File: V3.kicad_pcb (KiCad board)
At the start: 2 copper layers, 128.2 x 59 mm, 105 parts, among them IC1 TPS62840DLCR","TPS62840DLCR, J1 Conn_01x04, J2 Conn_01x04, J3 FFC2B28-24-G, J6 Conn_01x02, J7 Conn_01x02, Q1 FDN304P","FDN304P, Q2 FDN304P","FDN304P, Q3 FDN304P","FDN304P, Q4 FDN304P","FDN304P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

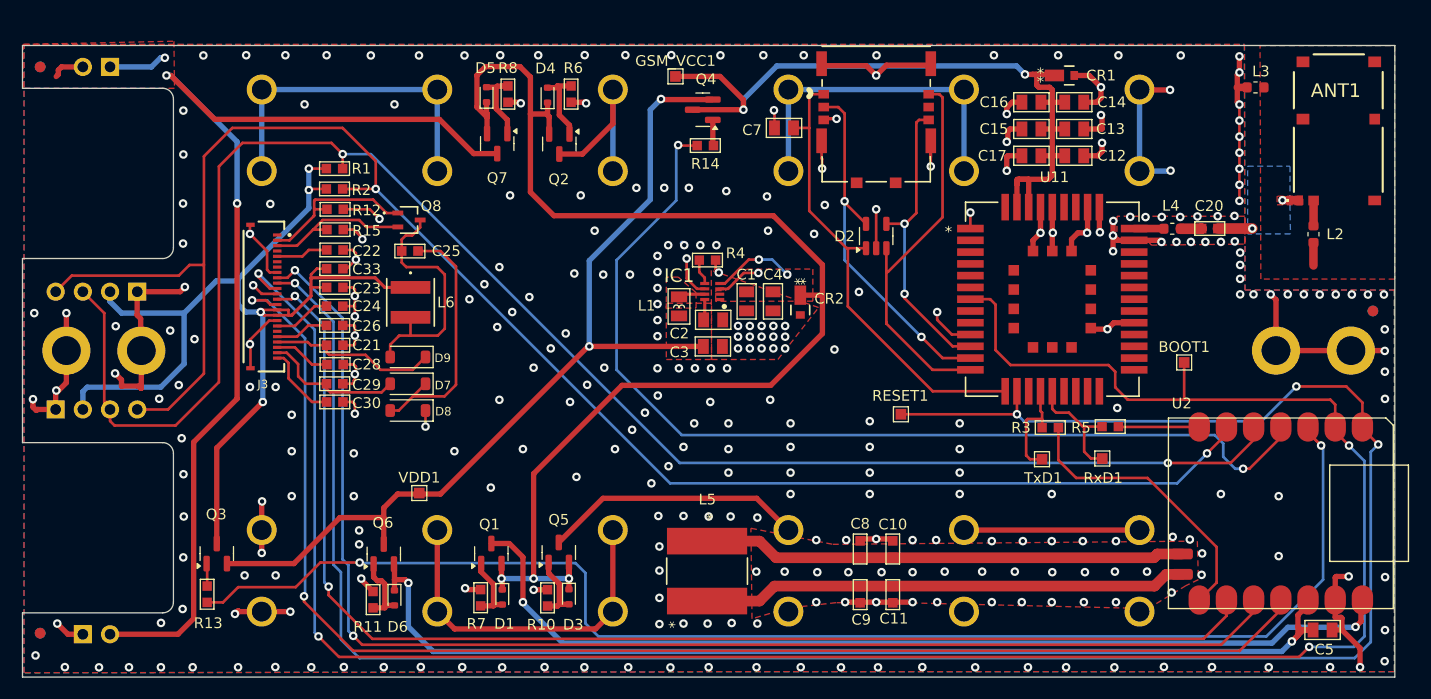
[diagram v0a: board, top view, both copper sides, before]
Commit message: add resisors to sim card, move TVS diode, add 3rd i2c header
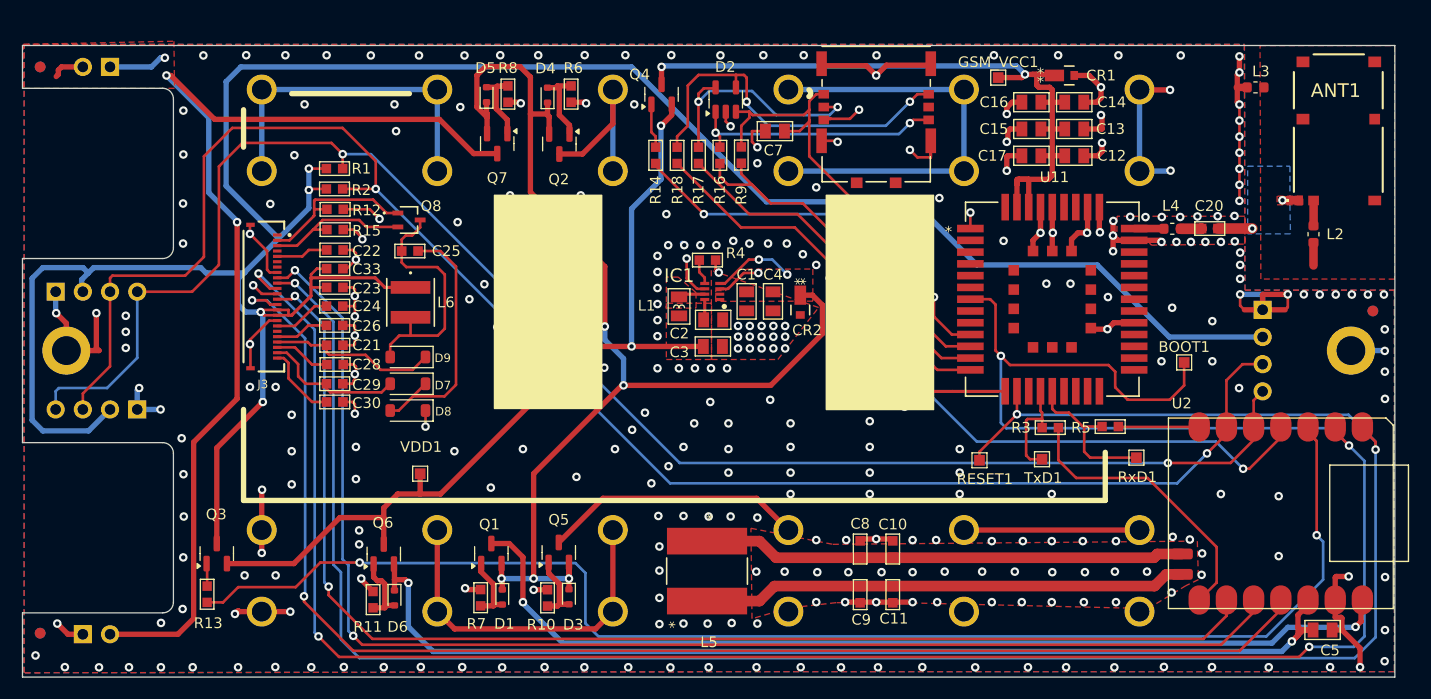
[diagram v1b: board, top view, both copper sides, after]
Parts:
- removed H3, H8: MountingHole_Pad_MP, MountingHole:MountingHole_2.7mm_M2.5_ISO14580_Pad
- added J4: Conn_01x04, Connector_PinSocket_2.54mm:PinSocket_1x04_P2.54mm_Vertical, B.Cu at (51.8, -3.81)
- added R16: 22R","22R, kicad_mod:R0603, F.Cu at (1.05, -18.2)
- added R17: 22R","22R, kicad_mod:R0603, F.Cu at (-0.95, -18.2)
- added R18: 22R","22R, kicad_mod:R0603, F.Cu at (-2.95, -18.2)
- added R9: 10K","RC0603JR-0710KL, kicad_mod:R0603, F.Cu at (3.05, -18.3)
- C10, C11: value ~ -> 3.6pF","CBR06C369B5GAC
- C5, C7: footprint OPL_Capacitor:C0805 -> kicad_mod:C0805
- C8, C9: value 335pF","GCM1885C2A331JA16D -> 51pF","06031U510GAT2A
- moved G*** 57.2 mm to (56.0, -17.0), turned to -90 degrees
- moved GSM_VCC1 30.2 mm to (27.1, -25.5)
- moved D2 19.0 mm to (1.60, -23.4)
- moved RESET1 8.51 mm to (25.3, 10.2)
- moved J1 7.62 mm to (-53.4, 5.50), turned to 90 degrees
- moved J2 7.62 mm to (-61.0, -5.50), turned to -90 degrees
- moved R14 4.73 mm to (-4.95, -18.2), turned to 90 degrees
- moved Q4 4.11 mm to (-4.40, -23.9), turned to 90 degrees
- moved RxD1 3.19 mm to (40.0, 10.0)
- moved VDD1 1.81 mm to (-26.9, 11.5)
- moved C7 0.90 mm to (6.19, -20.5)
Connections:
- D2 pad 1: SIM_VCC -> TVS_IO
- D2 pad 3: SIM_CLK -> SIM_VCC
- D2 pad 4: SIM_IO -> TVS_CLK
- D2 pad 5: SIM_RST -> TVS_RST
- J1 pad 3: SDA -> SCL
- J1 pad 4: SCL -> SDA
- J2 pad 3: SDA -> SCL
- J2 pad 4: SCL -> SDA
- U12 pad S2: SIM_RST -> TVS_RST
- U12 pad S3: SIM_CLK -> TVS_CLK
- U12 pad S6: SIM_IO -> TVS_IO
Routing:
- net CO2_VCC: track 99.8 -> 237.4 mm
- net TVS_CLK: track 0.00 -> 34.9 mm, vias 0 -> 2
- net TVS_IO: track 0.00 -> 24.0 mm, vias 0 -> 2
- net TVS_RST: track 0.00 -> 22.7 mm, vias 0 -> 2
- net DISPLAY_DC: track 205.5 -> 227.9 mm, vias 4 -> 5
- net SIM_VCC: track 43.7 -> 62.9 mm, vias 0 -> 2
- net GSM_PWR: track 93.0 -> 77.6 mm
- net +BATT: track 130.0 -> 118.1 mm, vias 5 -> 7
- net Net-(U7-Pad1): track 31.6 -> 40.4 mm
- net SIM_IO: track 27.9 -> 35.7 mm, vias 2 -> 0
- net SDA: track 158.0 -> 150.5 mm
- net GND: track 248.6 -> 241.7 mm, vias 325 -> 344
- net DISPLAY_RST: track 204.9 -> 198.1 mm, vias 4 -> 3
- net VDD: track 88.4 -> 83.8 mm
- net GSM_VCC: track 72.2 -> 69.0 mm
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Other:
- board text added: "ComplexityMadeSimple.com"
- board text removed: "ComplexityMadeSimple.com MoistureIQ V1.0"

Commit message: add resistors for sim card. Move componets from sticky pads, make extra room for sim card holder
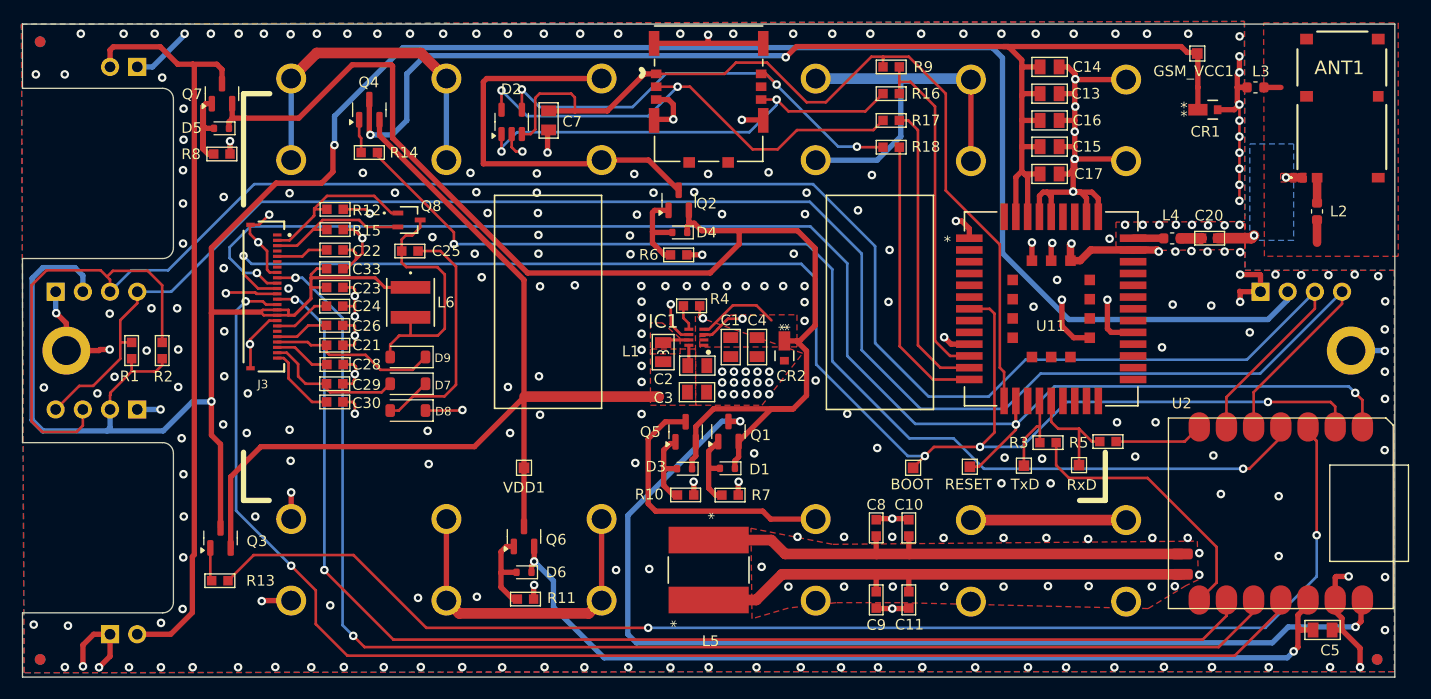
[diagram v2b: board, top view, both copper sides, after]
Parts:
- removed C12: 10uF","EMK212BJ106KG-T, kicad_mod:C0805
- moved FID4 32.6 mm to (62.5, 28.9)
- moved FID5 32.6 mm to (62.5, 28.9)
- moved G*** 32.2 mm to (55.0, 15.2)
- moved Q4 27.3 mm to (-31.7, -22.5)
- moved R8 27.3 mm to (-45.5, -18.4), turned to 180 degrees
- moved BOOT 27.2 mm to (19.1, 10.9)
- moved R14 26.8 mm to (-31.7, -18.5), turned to 180 degrees
- moved Q7 26.1 mm to (-45.5, -24.0), turned to 90 degrees
- moved R1 25.5 mm to (-53.9, 0.00), turned to -90 degrees
- moved R7 25.2 mm to (2.00, 13.5), turned to 180 degrees
- moved D5 25.0 mm to (-45.5, -20.8), turned to 180 degrees
- moved Q1 24.9 mm to (1.85, 7.56)
- moved D1 24.2 mm to (1.75, 11.0), turned to 180 degrees
- moved R2 22.1 mm to (-51.0, 0.00), turned to -90 degrees
- moved C7 21.2 mm to (-14.9, -21.5), turned to -90 degrees
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- renumbered BOOT1 to BOOT, RESET1 to RESET, RxD1 to RxD, TxD1 to TxD
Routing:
- net DISPLAY_DC: track 227.9 -> 141.5 mm, vias 5 -> 4
- net DISPLAY_RST: track 198.1 -> 141.1 mm
- net GSM_VCC: track 69.0 -> 122.1 mm
- net SCL: track 157.6 -> 190.7 mm, vias 2 -> 0
- net Vin3: track 100.6 -> 71.7 mm, vias 2 -> 0
- net GSM_PWR: track 77.6 -> 103.4 mm
- net TVS_RST: track 22.7 -> 45.1 mm
- net SIM_VCC: track 62.9 -> 85.3 mm, vias 2 -> 0
- net Vin2: track 17.0 -> 37.9 mm
- net TVS_IO: track 24.0 -> 42.4 mm
- net SDA: track 150.5 -> 165.9 mm, vias 2 -> 0
- net MCU_3V3: track 99.8 -> 85.3 mm
- net +BATT: track 118.1 -> 129.7 mm, vias 7 -> 0
- net VDD: track 83.8 -> 95.2 mm, vias 2 -> 0
- net SIM_CLK: track 35.4 -> 26.3 mm
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- removed copper zone on F.Cu, net Vin3
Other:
- board size 128.2 x 59 mm -> 128.2 x 61 mm

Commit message: ordred 23/10/2024
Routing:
- net GND: track 235.0 -> 240.2 mm, vias 304 -> 336
- net SIM_VCC: track 85.3 -> 89.3 mm
- net DISPLAY_SCK: track 117.7 -> 119.1 mm
- net CO2_VCC: track 238.8 -> 237.9 mm
- net GSM_VCC: track 122.1 -> 122.9 mm
- net TVS_RST: track 45.1 -> 46.0 mm
- net DISPLAY_DC: track 141.5 -> 140.7 mm
- net GSM_PWR: track 103.4 -> 102.8 mm
- net Net-(ANT1-FEED_(50_OHM)): track 5.02 -> 5.60 mm
- net MCU_3V3: track 85.3 -> 85.8 mm
- net DISPLAY_MOSI: track 129.8 -> 130.4 mm

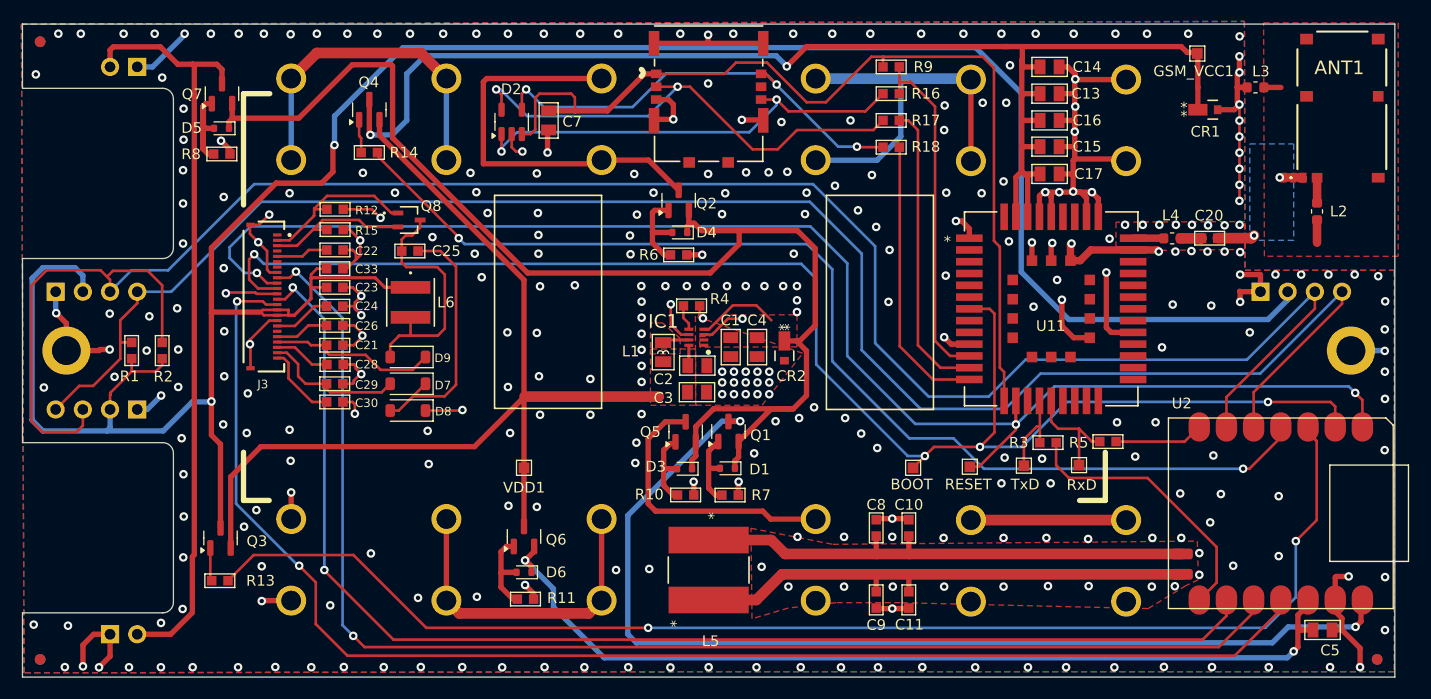
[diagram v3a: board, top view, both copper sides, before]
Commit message: change OR ring to diodes
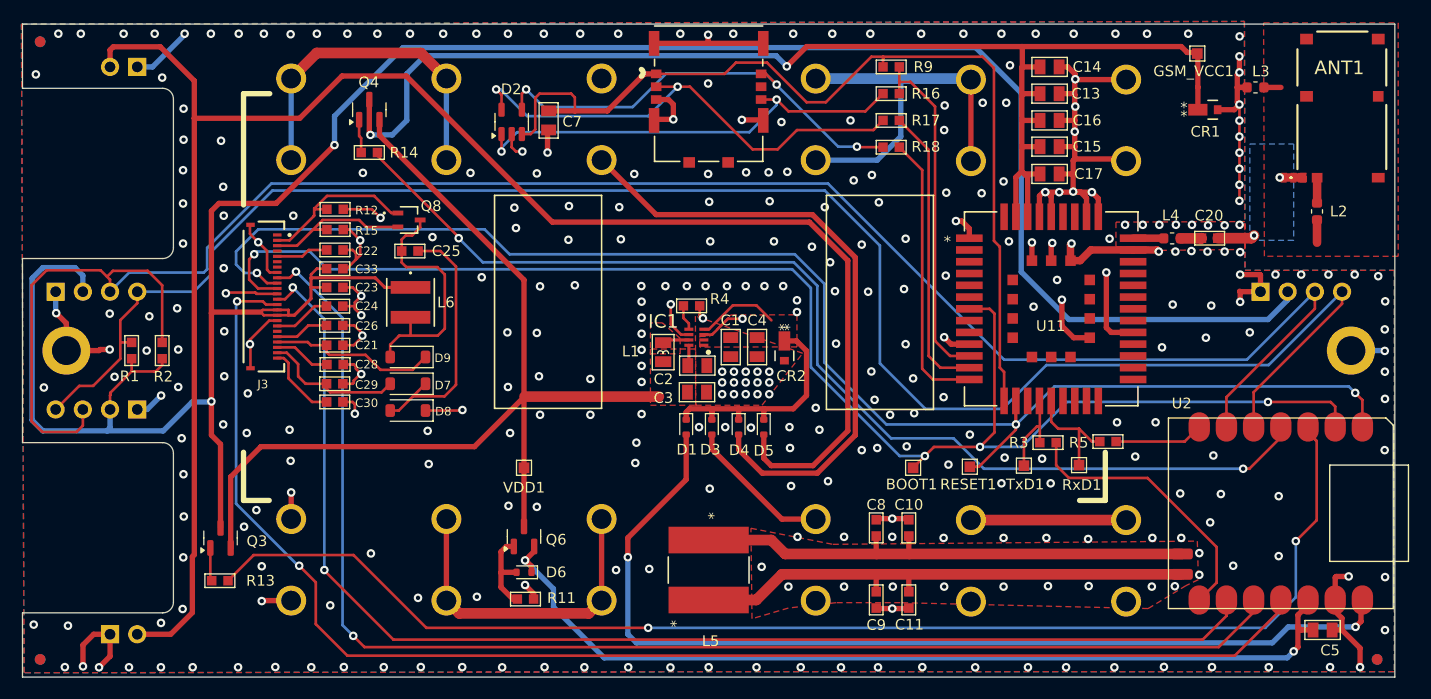
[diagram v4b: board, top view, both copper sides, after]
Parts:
- removed Q1, Q2, Q5, Q7: FDN304P","FDN304P, Package_TO_SOT_SMD:SOT-23
- removed R10, R6, R7, R8: 100K","RC0603JR-07100KL, kicad_mod:R0603
- moved D5 57.8 mm to (5.15, 7.15), turned to -90 degrees
- moved D4 19.0 mm to (2.80, 7.15), turned to -90 degrees
- moved D1 5.44 mm to (-2.10, 7.15), turned to -90 degrees
- moved D3 4.65 mm to (0.30, 7.15), turned to -90 degrees
- renumbered BOOT to BOOT1, RESET to RESET1, RxD to RxD1, TxD to TxD1
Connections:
- D1 pad 2: Net-(D1-A) -> USB_5V
- D3 pad 2: Net-(D3-A) -> Vin1
- D4 pad 2: Net-(D4-A) -> Vin2
- D5 pad 2: Net-(D5-A) -> Vin3
- U10 pad 1: Vin2 -> unconnected-(U10-Pad1)
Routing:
- net +BATT: track 129.7 -> 30.1 mm
- net Vin3: track 71.7 -> 164.1 mm
- net Vin2: track 37.9 -> 58.7 mm
- net Vin1: track 26.5 -> 13.8 mm
- net Net-(D5-A): track 11.1 -> 0.00 mm
- net Net-(D4-A): track 8.46 -> 0.00 mm
- net GND: track 240.2 -> 232.5 mm, vias 336 -> 348
- net Net-(D3-A): track 7.63 -> 0.00 mm
- net Net-(D1-A): track 7.30 -> 0.00 mm
- net SCL: track 190.7 -> 183.7 mm
- net USB_5V: track 97.9 -> 92.4 mm
- net SDA: track 165.9 -> 169.2 mm
- net DISPLAY_RST: track 141.1 -> 139.0 mm
- net GSM_VCC: track 122.9 -> 121.7 mm
- net GSM_PWR: track 102.8 -> 102.1 mm
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
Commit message: replace reverse polarity mosfets with diodes
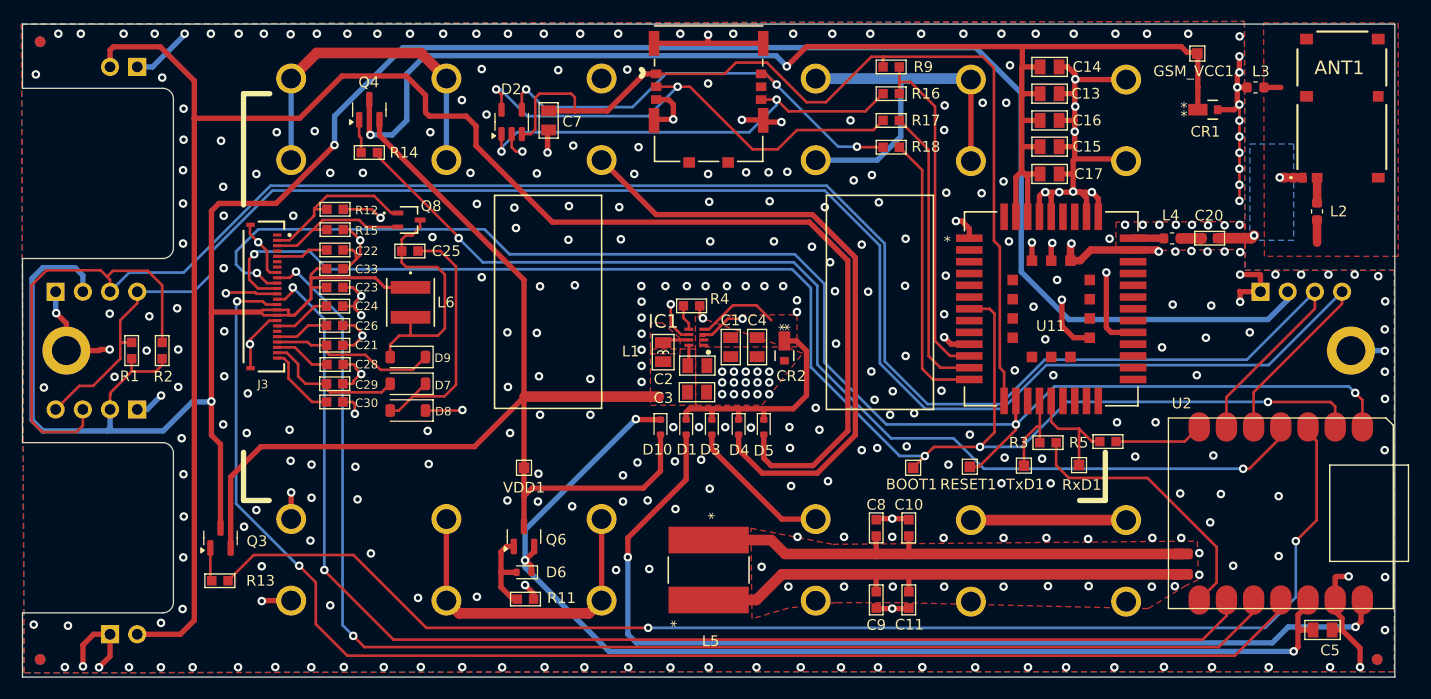
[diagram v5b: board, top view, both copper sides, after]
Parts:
- added D10: NSR0520V2","NSR0520V2, Diode_SMD:D_SOD-523, F.Cu at (-4.50, 7.15)
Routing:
- net MCU_3V3: track 85.8 -> 104.5 mm, vias 2 -> 3
- net VDD: track 95.2 -> 112.3 mm
- net SCL: track 183.7 -> 192.3 mm
- net Vin3: track 164.1 -> 166.6 mm
- net GND: track 232.5 -> 234.3 mm, vias 348 -> 379

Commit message: revision to review with ideal diode oring
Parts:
- removed Q6: FDN304P","FDN304P, Package_TO_SOT_SMD:SOT-23
- removed R11: 100K","RC0603JR-07100KL, kicad_mod:R0603
- added C12: 1uF",CC0603KRX5R7BB105, kicad_mod:C0603, F.Cu at (-12.0, 9.50)
- added C18: 1uF",CC0603KRX5R7BB105, kicad_mod:C0603, F.Cu at (6.00, 9.50)
- added C6: 1uF",CC0603KRX5R7BB105, kicad_mod:C0603, F.Cu at (-3.00, 9.50)
- added R6: 10K","RC0603JR-0710KL, kicad_mod:R0603, F.Cu at (3.00, 9.50)
- added R7: 10K","RC0603JR-0710KL, kicad_mod:R0603, F.Cu at (12.0, 9.50)
- added R8: 10K","RC0603JR-0710KL, kicad_mod:R0603, F.Cu at (-6.00, 9.50)
- added U1: LM66100DCK, Package_TO_SOT_SMD:SOT-363_SC-70-6, F.Cu at (-9.00, 9.50)
- added U18: LM66100DCK, Package_TO_SOT_SMD:SOT-363_SC-70-6, F.Cu at (9.00, 9.50)
- added U3: LM66100DCK, Package_TO_SOT_SMD:SOT-363_SC-70-6, F.Cu at (0.00, 9.50)
- moved D5 64.0 mm to (-49.0, -27.0)
- moved D6 32.5 mm to (-49.0, 27.6), turned to -90 degrees
- moved J6 2.73 mm to (-55.9, -27.5)
- moved J7 2.73 mm to (-58.5, 27.5)
- moved D10 2.46 mm to (-6.00, 5.20)
- moved D1 2.15 mm to (-3.00, 5.20)
- moved C1 2.09 mm to (2.32, -2.40)
- moved C2 2.09 mm to (-0.80, -0.67)
- moved C3 2.09 mm to (-0.83, 1.82)
- moved C4 2.09 mm to (4.79, -2.40)
- moved CR2 2.09 mm to (7.34, -2.32)
- moved IC1 2.09 mm to (-0.89, -3.32)
- moved L1 2.09 mm to (-3.99, -1.93)
- moved R4 2.09 mm to (-1.33, -6.25)
- moved D3 1.97 mm to (0.00, 5.20)
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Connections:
- D5 pad 2: Vin3 -> Net-(D5-A)
- D6 pad 1: MCU_3V3 -> +BATT
- J6 pad 2: Vin3 -> Net-(D5-A)
- J7 pad 2: Vin3 -> Net-(D6-A)
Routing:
- net +BATT: track 30.1 -> 204.7 mm
- net Vin3: track 166.6 -> 0.00 mm
- net TVS_CLK: track 42.1 -> 59.6 mm, vias 3 -> 2
- net Net-(D5-A): track 0.00 -> 11.7 mm
- net DISPLAY_MOSI: track 130.4 -> 140.7 mm
- net Vin1: track 13.8 -> 21.9 mm
- net VDD: track 112.3 -> 104.6 mm
- net TVS_RST: track 46.0 -> 53.2 mm, vias 2 -> 0
- net Net-(U7-Pad1): track 36.0 -> 29.4 mm
- net DISPLAY_DC: track 140.6 -> 146.9 mm
- net MCU_3V3: track 104.5 -> 98.2 mm, vias 3 -> 2
- net CO2_VCC: track 238.5 -> 244.7 mm
- net Net-(U18-~{CE}): track 0.00 -> 5.65 mm
- net Net-(U1-~{CE}): track 0.00 -> 5.65 mm
- net Net-(U3-~{CE}): track 0.00 -> 5.60 mm
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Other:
- board text added: "5V"
- board text added: "Battery Bank 1 1.2-1.5V AA"
- board text added: "Battery Bank 2 1.2-1.5V AA"
- board text added: "INPUT"

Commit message: pre order review
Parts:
- added REF**: UKCA-Logo_6x6mm_SilkScreen, Symbol:UKCA-Logo_6x6mm_SilkScreen, B.Cu at (57.4, -25.0)
- added REF**: CE-Logo_8.5x6mm_SilkScreen, Symbol:CE-Logo_8.5x6mm_SilkScreen, B.Cu at (57.5, -15.4)
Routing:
- net CO2_VCC: track 244.7 -> 250.6 mm
- net DISPLAY_DC: track 146.9 -> 151.4 mm
- net +BATT: track 204.7 -> 201.6 mm
- net GDR: track 14.9 -> 17.0 mm
- net GND: track 239.7 -> 241.6 mm, vias 325 -> 333
- net DISPLAY_BUSY: track 125.9 -> 124.6 mm
- net DISPLAY_RST: track 139.4 -> 140.4 mm
- net MCU_3V3: track 98.2 -> 97.6 mm
- net RESE: track 13.8 -> 14.4 mm
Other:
- board text added: "AA"
- board text removed: "Battery Bank 1 1.2-1.5V AA"
- board text removed: "Battery Bank 2 1.2-1.5V AA"
